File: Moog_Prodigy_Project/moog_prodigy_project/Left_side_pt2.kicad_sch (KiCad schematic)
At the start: 93 parts, among them Q1 CA3046, Q11 BC107, Q17 BC549, Q2 CA3046, SW3 SW_Slide_DPDT, U10 AD8066ARM, U22 +12V, U23 +12V, U24 +12V, U25 +12V, U26 +12V, U27 +12V, U28 +12V, U29 +12V, U2B1 OPA134, U30 +12V, U31 +12V, U32 +12V, U33 +12V, U42 +12V, U43 -12V, U44 -12V, U45 -12V, U46 -12V, U47 -12V, U48 -12V, U49 -12V, U4B1 OPA134, U50 -12V, U51 -12V, U52 -12V, U53 +12V, U54 -12V, U8 NE5532, U9 LT1011CN8

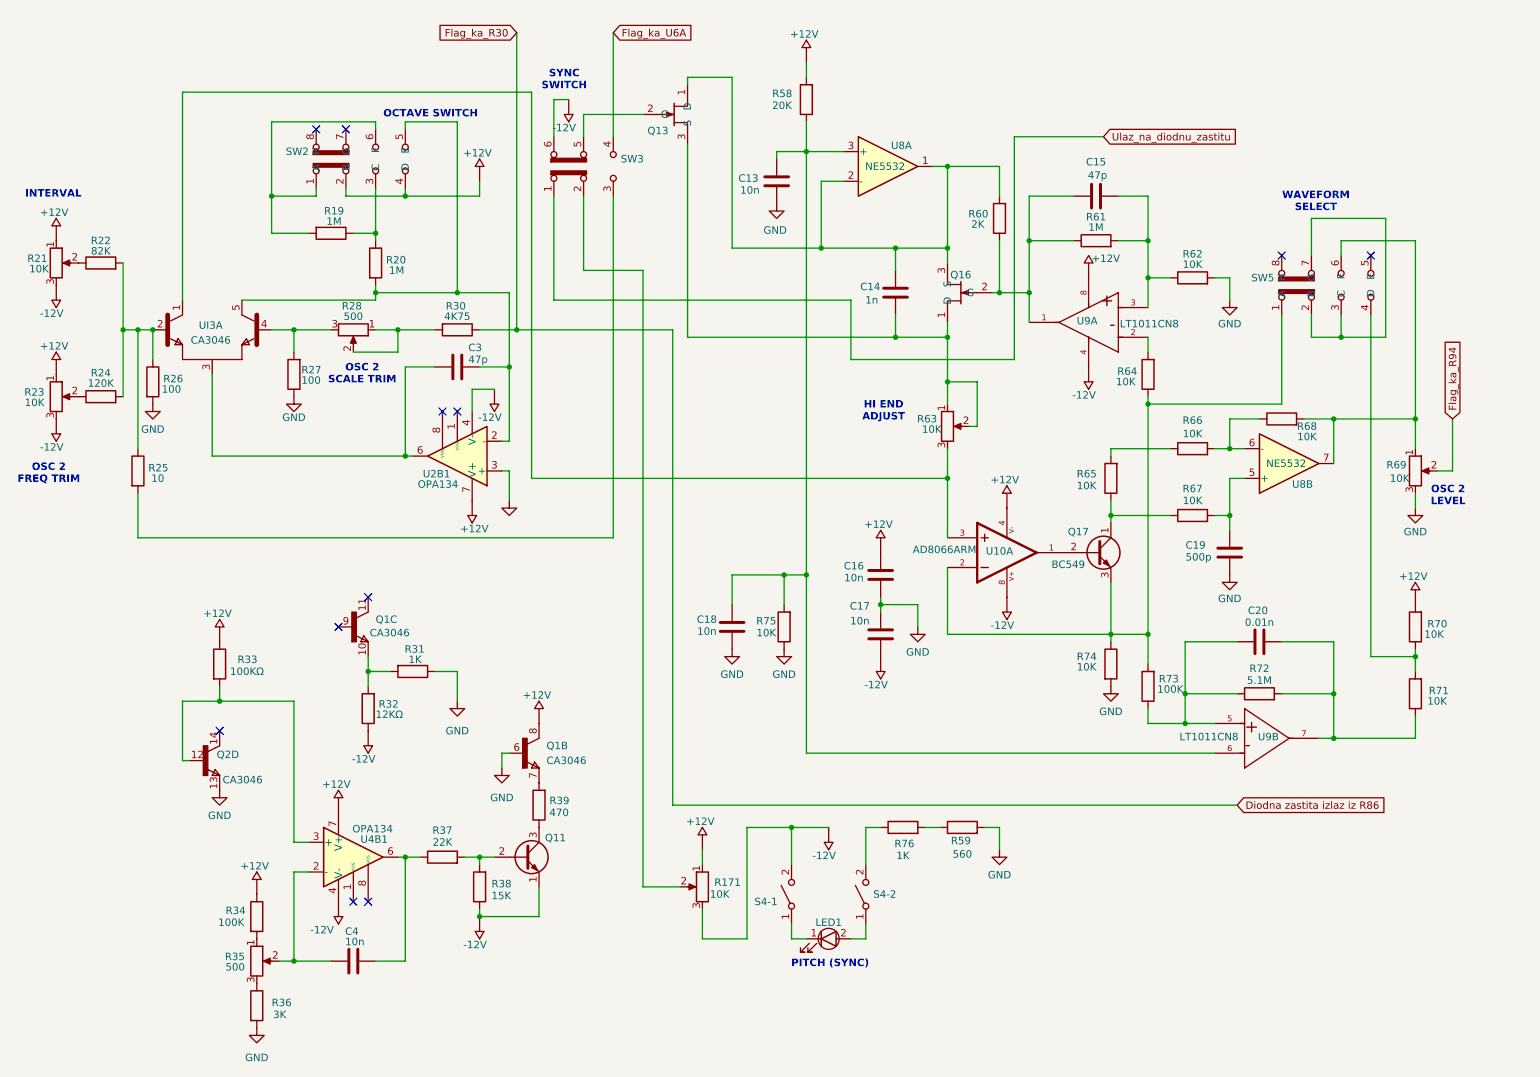
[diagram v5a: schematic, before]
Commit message: Footprint update new 28.04.2026
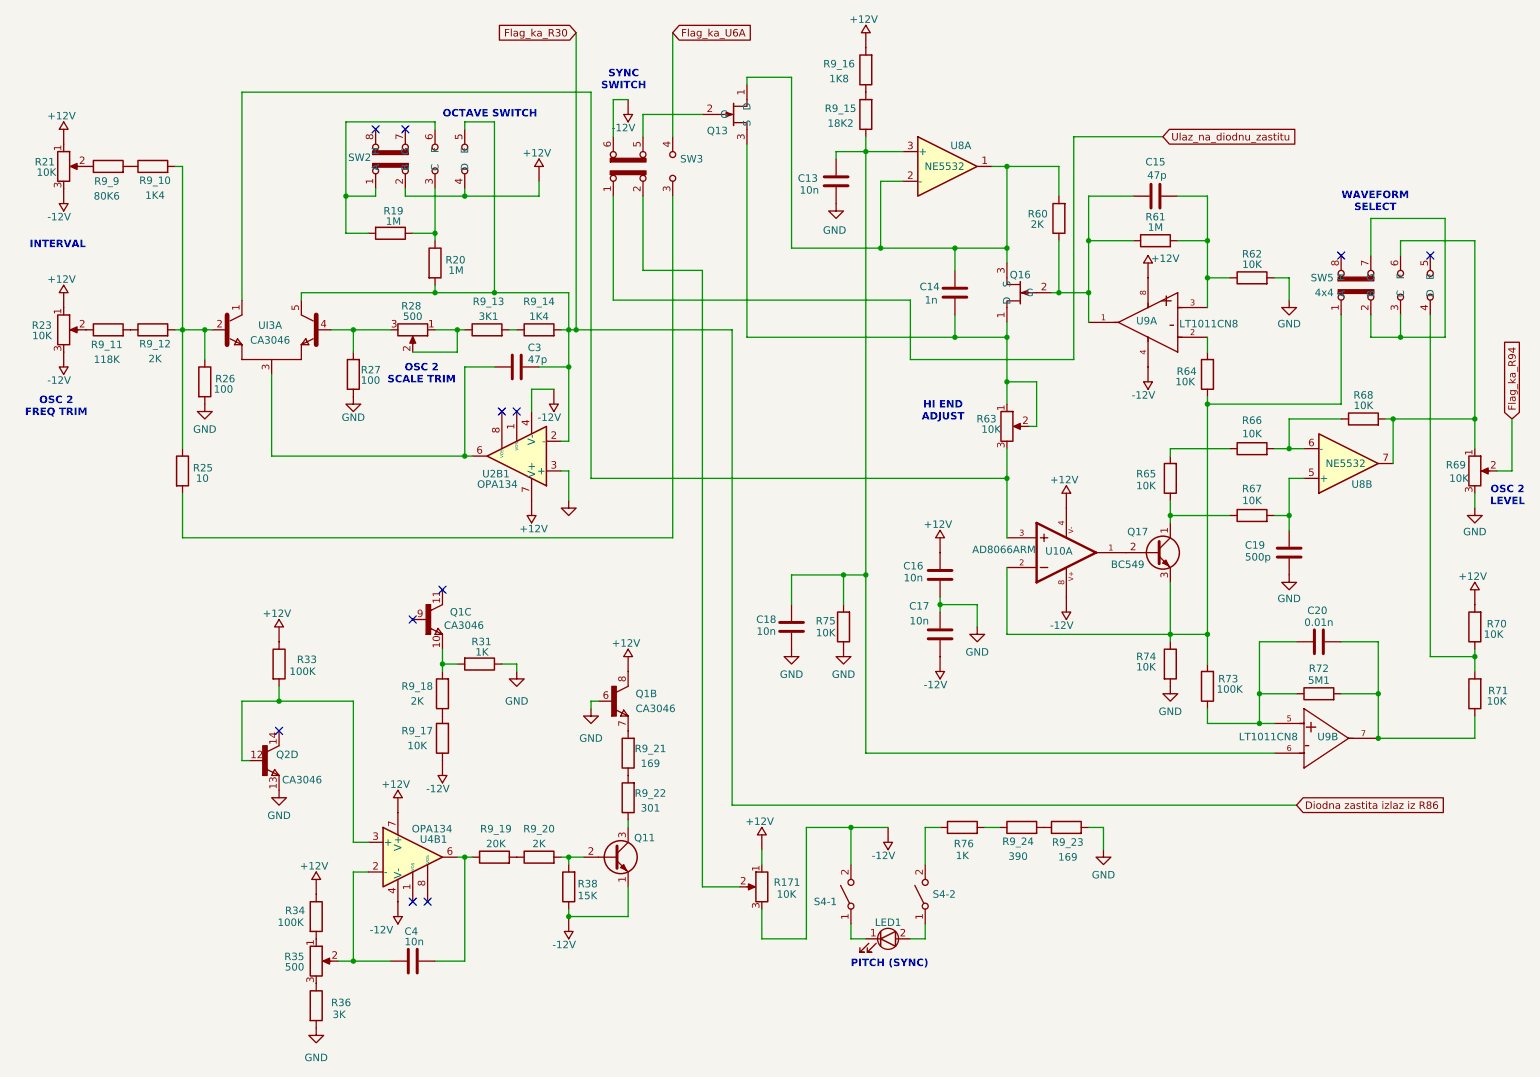
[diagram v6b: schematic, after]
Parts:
- removed R22: 82K, symbol Device:R
- removed R24: 120K, symbol Device:R
- removed R30: 4K75, symbol Device:R
- removed R32: 12KΩ, symbol Device:R
- removed R37: 22K, symbol Device:R
- removed R39: 470, symbol Device:R
- removed R58: 20K, symbol Device:R
- removed R59: 560, symbol Device:R
- added R9_10, R9_14: 1K4, Resistor_THT:R_Axial_DIN0207_L6.3mm_D2.5mm_P10.16mm_Horizontal, symbol Device:R
- added R9_11: 118K, Resistor_THT:R_Axial_DIN0207_L6.3mm_D2.5mm_P10.16mm_Horizontal, symbol Device:R
- added R9_12, R9_18, R9_20: 2K, Resistor_THT:R_Axial_DIN0207_L6.3mm_D2.5mm_P10.16mm_Horizontal, symbol Device:R
- added R9_13: 3K1, Resistor_THT:R_Axial_DIN0207_L6.3mm_D2.5mm_P10.16mm_Horizontal, symbol Device:R
- added R9_15: 18K2, Resistor_THT:R_Axial_DIN0207_L6.3mm_D2.5mm_P10.16mm_Horizontal, symbol Device:R
- added R9_16: 1K8, Resistor_THT:R_Axial_DIN0207_L6.3mm_D2.5mm_P10.16mm_Horizontal, symbol Device:R
- added R9_17: 10K, Resistor_THT:R_Axial_DIN0207_L6.3mm_D2.5mm_P10.16mm_Horizontal, symbol Device:R
- added R9_19: 20K, Resistor_THT:R_Axial_DIN0207_L6.3mm_D2.5mm_P10.16mm_Horizontal, symbol Device:R
- added R9_21, R9_23: 169, Resistor_THT:R_Axial_DIN0207_L6.3mm_D2.5mm_P10.16mm_Horizontal, symbol Device:R
- added R9_22: 301, Resistor_THT:R_Axial_DIN0207_L6.3mm_D2.5mm_P10.16mm_Horizontal, symbol Device:R
- added R9_24: 390, Resistor_THT:R_Axial_DIN0207_L6.3mm_D2.5mm_P10.16mm_Horizontal, symbol Device:R
- added R9_9: 80K6, Resistor_THT:R_Axial_DIN0207_L6.3mm_D2.5mm_P10.16mm_Horizontal, symbol Device:R
- C13, C14, C15, C16, C17, C18, C19, C20, C3, C4: footprint (none) -> Capacitor_THT:C_Disc_D5.0mm_W2.5mm_P2.50mm
- LED1: value ~ -> LED_Diode; footprint (none) -> WP7113LGD:LED_WP7113LGD
- Q1, Q2: footprint (none) -> CA3046:DIL14
- Q13, Q16: value ~ -> BF256C
- R171, R19, R20, R21, R23, R25, R26, R27, R28, R31, R34, R35, R36, R38, R60, R61, R62, R63, R64, R65, R66, R67, R68, R69, R70, R71, R73, R74, R75, R76: footprint (none) -> Resistor_THT:R_Axial_DIN0207_L6.3mm_D2.5mm_P10.16mm_Horizontal
- R33: value 100KΩ -> 100K; footprint (none) -> Resistor_THT:R_Axial_DIN0207_L6.3mm_D2.5mm_P10.16mm_Horizontal
- R72: value 5.1M -> 5M1; footprint (none) -> Resistor_THT:R_Axial_DIN0207_L6.3mm_D2.5mm_P10.16mm_Horizontal
- S4-1, S4-2: footprint (none) -> L101011ML04Q_1x1:SW_L101011ML04Q
- SW2, SW5: value ~ -> 4x4; footprint (none) -> SLW-1575662-5A-S-D_Switch_4x4:SW_SLW-1575662-5A-S-D
- SW3: footprint (none) -> CL-SB-22A-02T_3x3:SW_CL-SB-22A-02T
- U8: footprint (none) -> NE5532AP:DIP794W45P254L1016H508Q8
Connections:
- net Diodna zastita izlaz iz R86: now also C3.2, R20.2, SW2.5 (E), U2B1.2 (-), UI3.5, R9_14.2
- net GND: now also R9_23.2
- net at R21.2: now also R9_9.1
- net at R25.1, R26.1, UI3.2: now also R9_10.2, R9_12.2
- net at R76.2: now also R9_24.1
- net at R28.1, R28.2: now also R9_13.1
- net at C13.2, C18.2, R75.2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: now also R9_15.1
- net at U24.: now also R9_16.2
- net at C4.2, U4B1.6: now also R9_19.1
- net at Q11.2 (B), R38.2: now also R9_20.2
- net at Q1.10, R31.2: now also R9_18.2
- net at Q11.3 (C): now also R9_22.1
- net at Q1.7: now also R9_21.2
- net at U48.: now also R9_17.1
- net at R23.2: now also R9_11.1
- new net: R9_23.1, R9_24.2
- new net: R9_19.2, R9_20.1
- new net: R9_10.1, R9_9.2
- new net: R9_15.2, R9_16.1
- new net: R9_13.2, R9_14.1
- new net: R9_17.2, R9_18.1
- new net: R9_11.2, R9_12.1
- new net: R9_21.1, R9_22.2
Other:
- moved on the sheet: C13, C14, C15, C16, C17, C18, C19, C20, C3, C4, LED1, Q11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

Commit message: Footprints import new 29.04.2026
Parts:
- U2B1, U4B1: footprint (none) -> OPA134PA:DIP794W45P254L959H508Q8
- U9: footprint Package_DIP:DIP-8_W7.62mm_Socket -> L101011ML04Q_1x1:SW_L101011ML04Q
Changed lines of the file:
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@@
 			)
 		)
-		(property "Footprint" "Package_DIP:DIP-8_W7.62mm_Socket"
+		(property "Footprint" "L101011ML04Q_1x1:SW_L101011ML04Q"
 			(at 215.9 63.5 0)
 			(effects
@@
 			)
 		)
-		(property "Footprint" ""
+		(property "Footprint" "OPA134PA:DIP794W45P254L959H508Q8"
 			(at 81.28 156.21 0)
 			(effects
@@
 			)
 		)
-		(property "Footprint" ""
+		(property "Footprint" "OPA134PA:DIP794W45P254L959H508Q8"
 			(at 96.52 90.17 0)
 			(effects
@@
 			)
 		)
-		(property "Footprint" "Package_DIP:DIP-8_W7.62mm_Socket"
+		(property "Footprint" "L101011ML04Q_1x1:SW_L101011ML04Q"
 			(at 227.33 134.62 0)
 			(effects
